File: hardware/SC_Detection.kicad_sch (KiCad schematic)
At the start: 86 parts, among them U15 LT1678CS8#PBF, U16 LT1678CS8#PBF, U17 LM211DRG4, U18 LM211DRG4, U19 LM211DRG4, U20 LM211DRG4

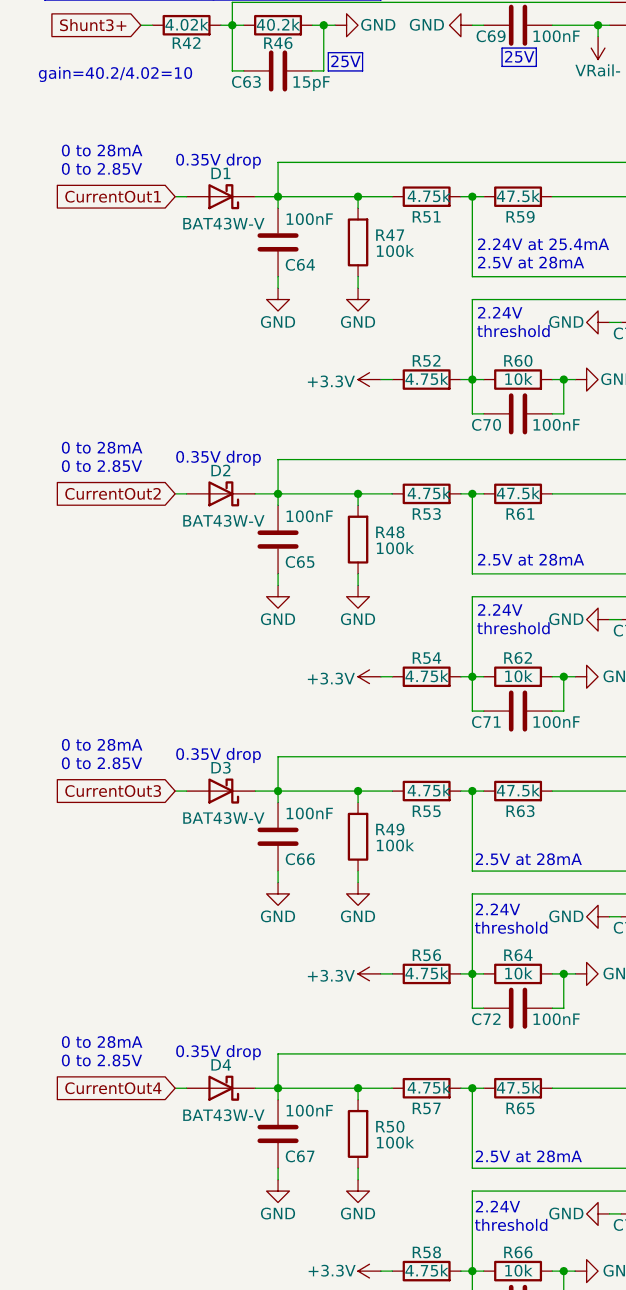
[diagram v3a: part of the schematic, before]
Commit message: Updating some footprints
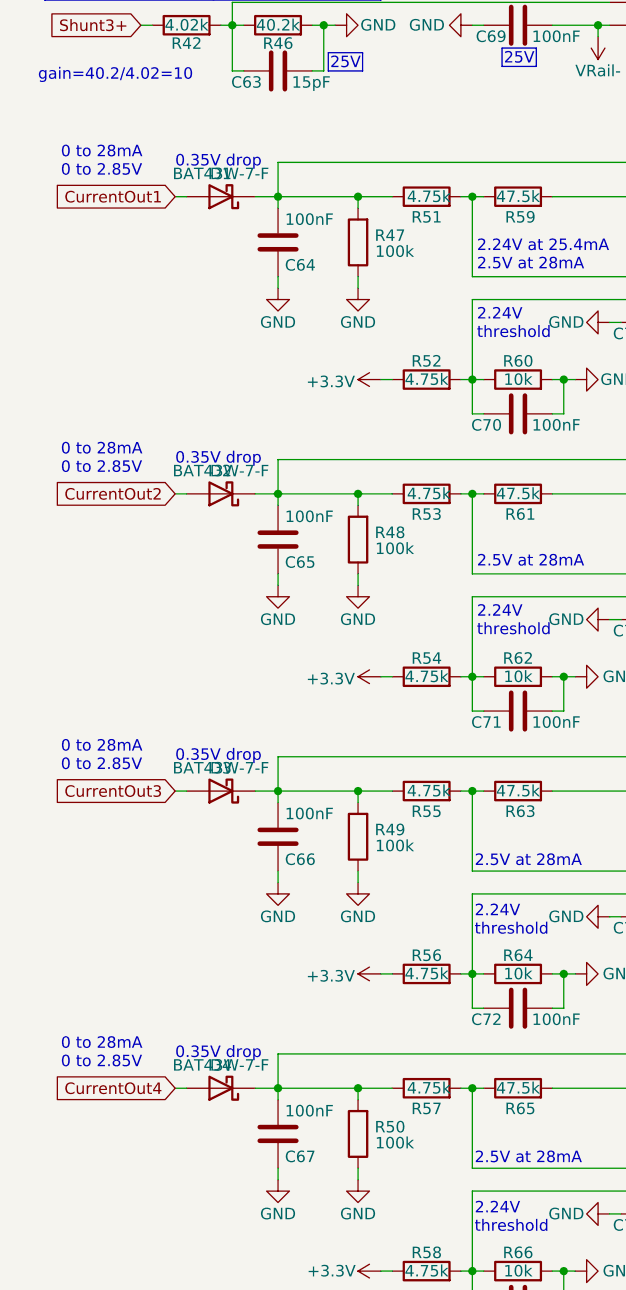
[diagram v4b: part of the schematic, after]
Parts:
- C60, C61, C62, C63, C64, C65, C66, C67, C68, C69, C70, C71, C72, C73, C74, C75, C76, C77, C78, C79, C80, C81, C82, C83, C84, C85, C86, C87, C88, C89, C90, C91: footprint Capacitor_SMD:C_0402_1005Metric -> Capacitor_SMD:C_0603_1608Metric; symbol harp.device.quad.dac:C -> harp.device.quad.dac:C_0603
- D1, D2, D3, D4: value BAT43W-V -> BAT43W-7-F
- R39, R40, R41, R42, R43, R44, R45, R46, R47, R48, R49, R50, R51, R52, R53, R54, R55, R56, R57, R58, R59, R60, R61, R62, R63, R64, R65, R66, R67, R68, R69, R70, R71, R72, R73, R74, R75, R76, R77, R78, R79, R80, R81, R82: footprint Resistor_SMD:R_0402_1005Metric -> Resistor_SMD:R_0603_1608Metric; symbol harp.device.quad.dac:R -> harp.device.quad.dac:R_0603
- U15, U16: footprint SOIC127P599X175-8N -> harp.device.quad.dac.kicad:SOIC127P599X175-8N
- U17, U18, U19, U20: footprint SOIC127P600X175-8N -> harp.device.quad.dac.kicad:SOIC127P600X175-8N

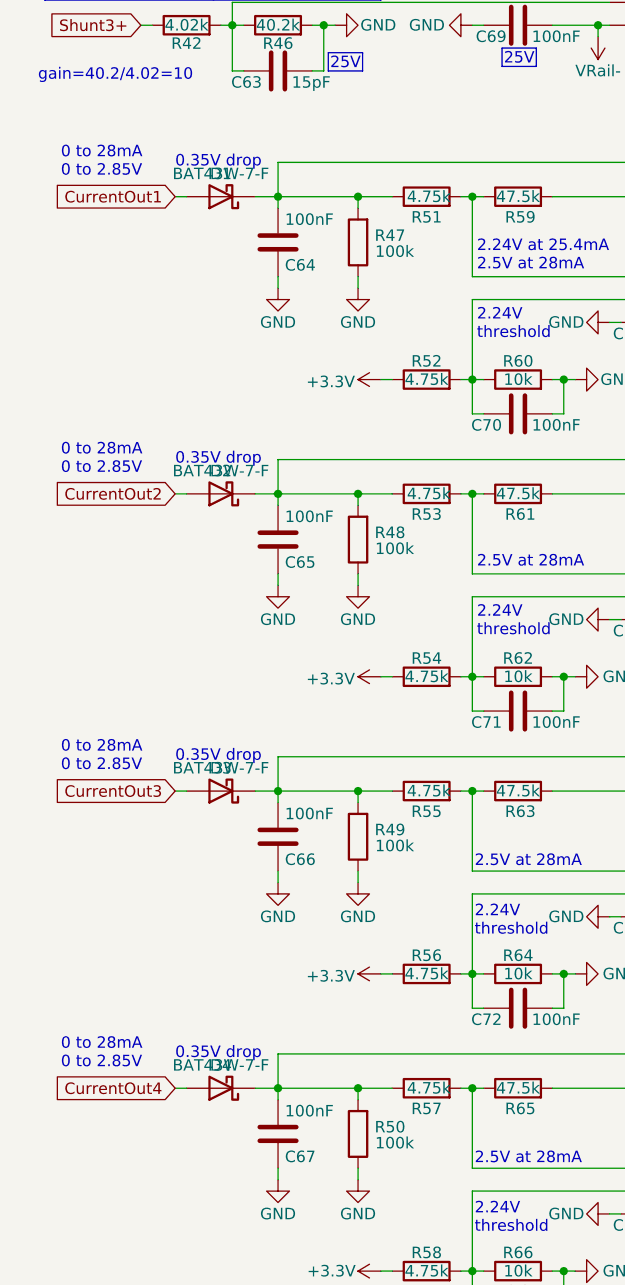
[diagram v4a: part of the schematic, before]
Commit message: Jumpers and interstages connections + added zeners to supply sections + justified text
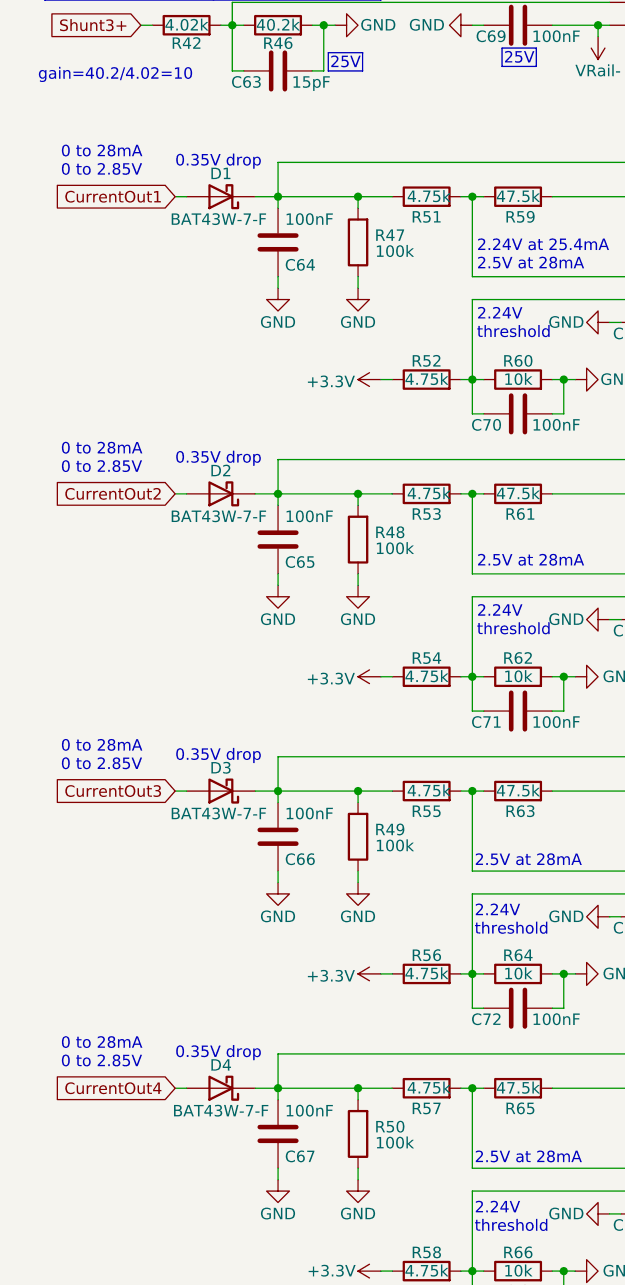
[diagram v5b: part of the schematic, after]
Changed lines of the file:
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@@
 		)
 		(property "Value" "BAT43W-7-F"
-			(at 33.02 168.91 0)
+			(at 33.02 173.99 0)
 			(effects
 				(font
@@
 		)
 		(property "Value" "BAT43W-7-F"
-			(at 33.02 135.89 0)
+			(at 32.766 140.97 0)
 			(effects
 				(font
@@
 		)
 		(property "Value" "BAT43W-7-F"
-			(at 33.02 69.85 0)
+			(at 32.766 74.93 0)
 			(effects
 				(font
@@
 		)
 		(property "Value" "BAT43W-7-F"
-			(at 33.02 102.87 0)
+			(at 32.766 107.95 0)
 			(effects
 				(font

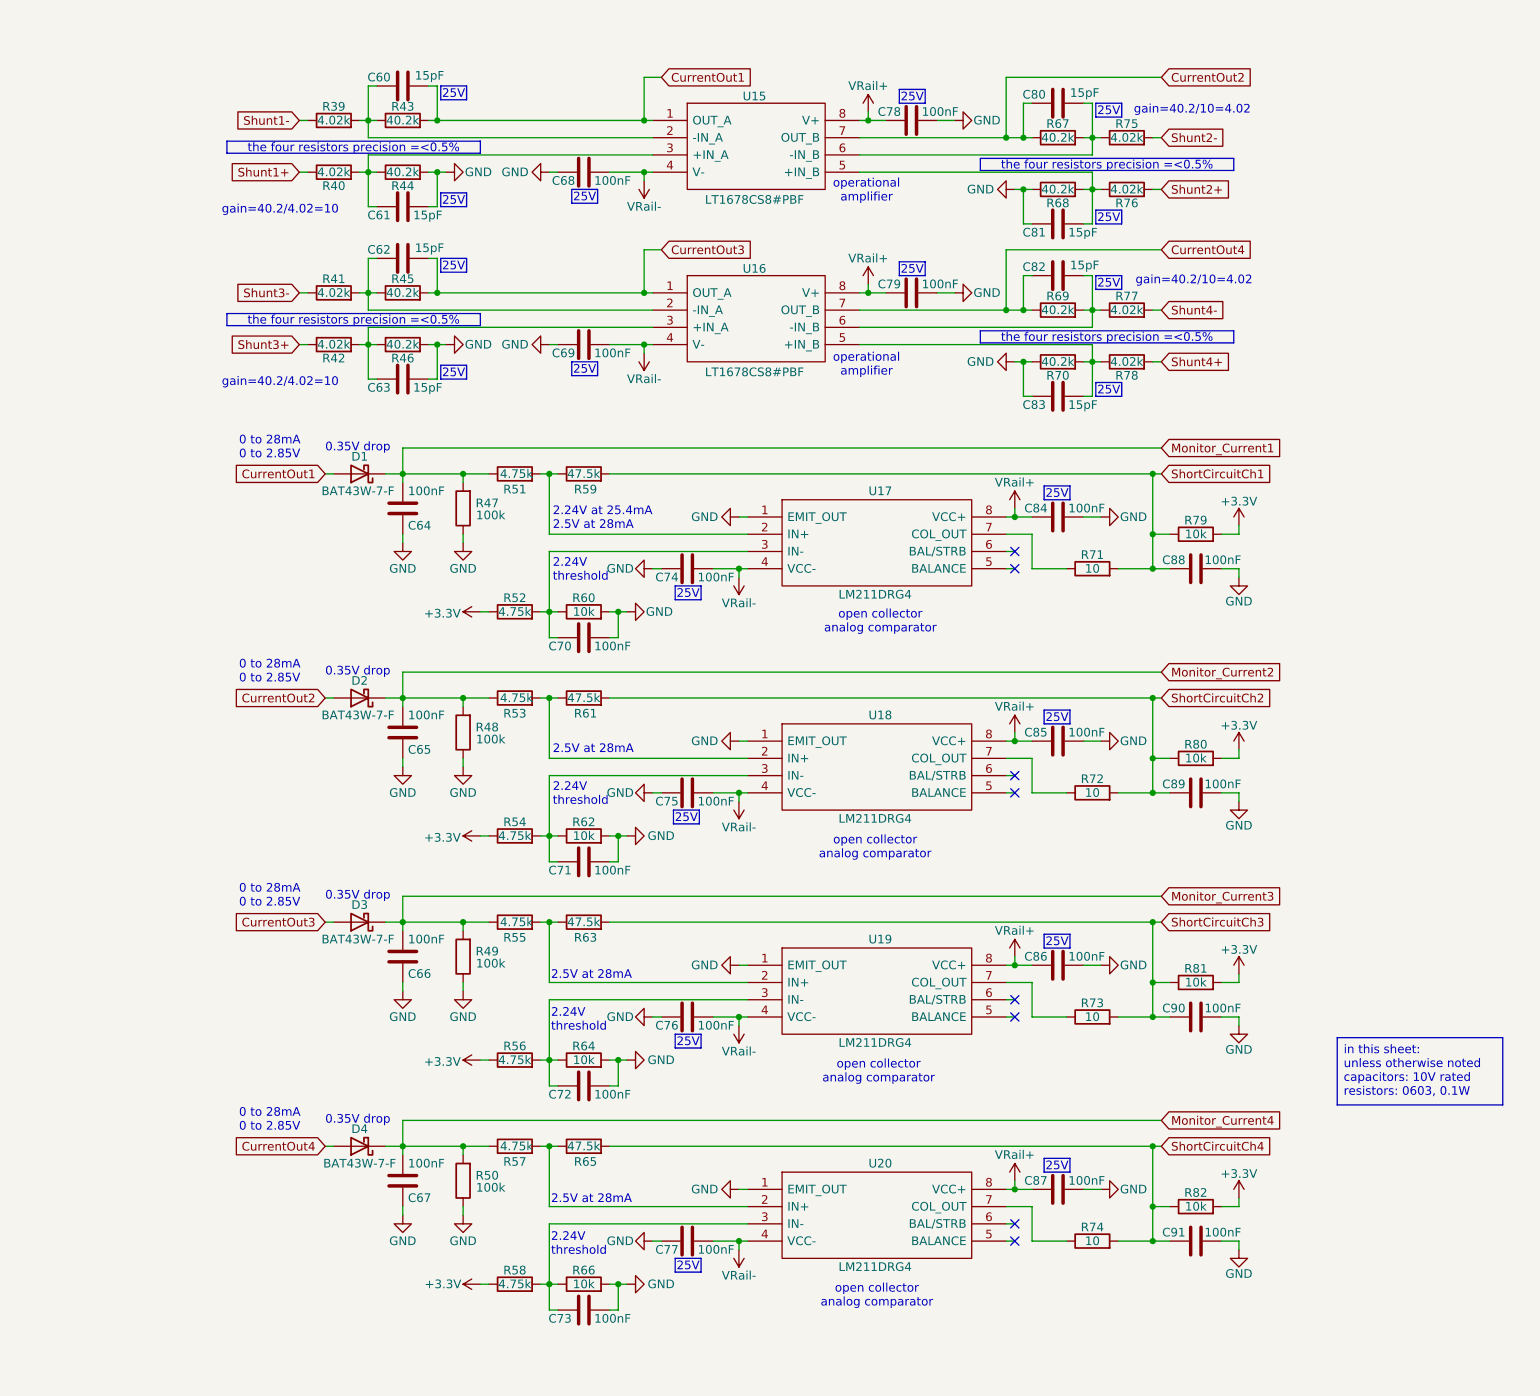
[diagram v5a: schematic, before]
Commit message: The part designators have been reannotated.
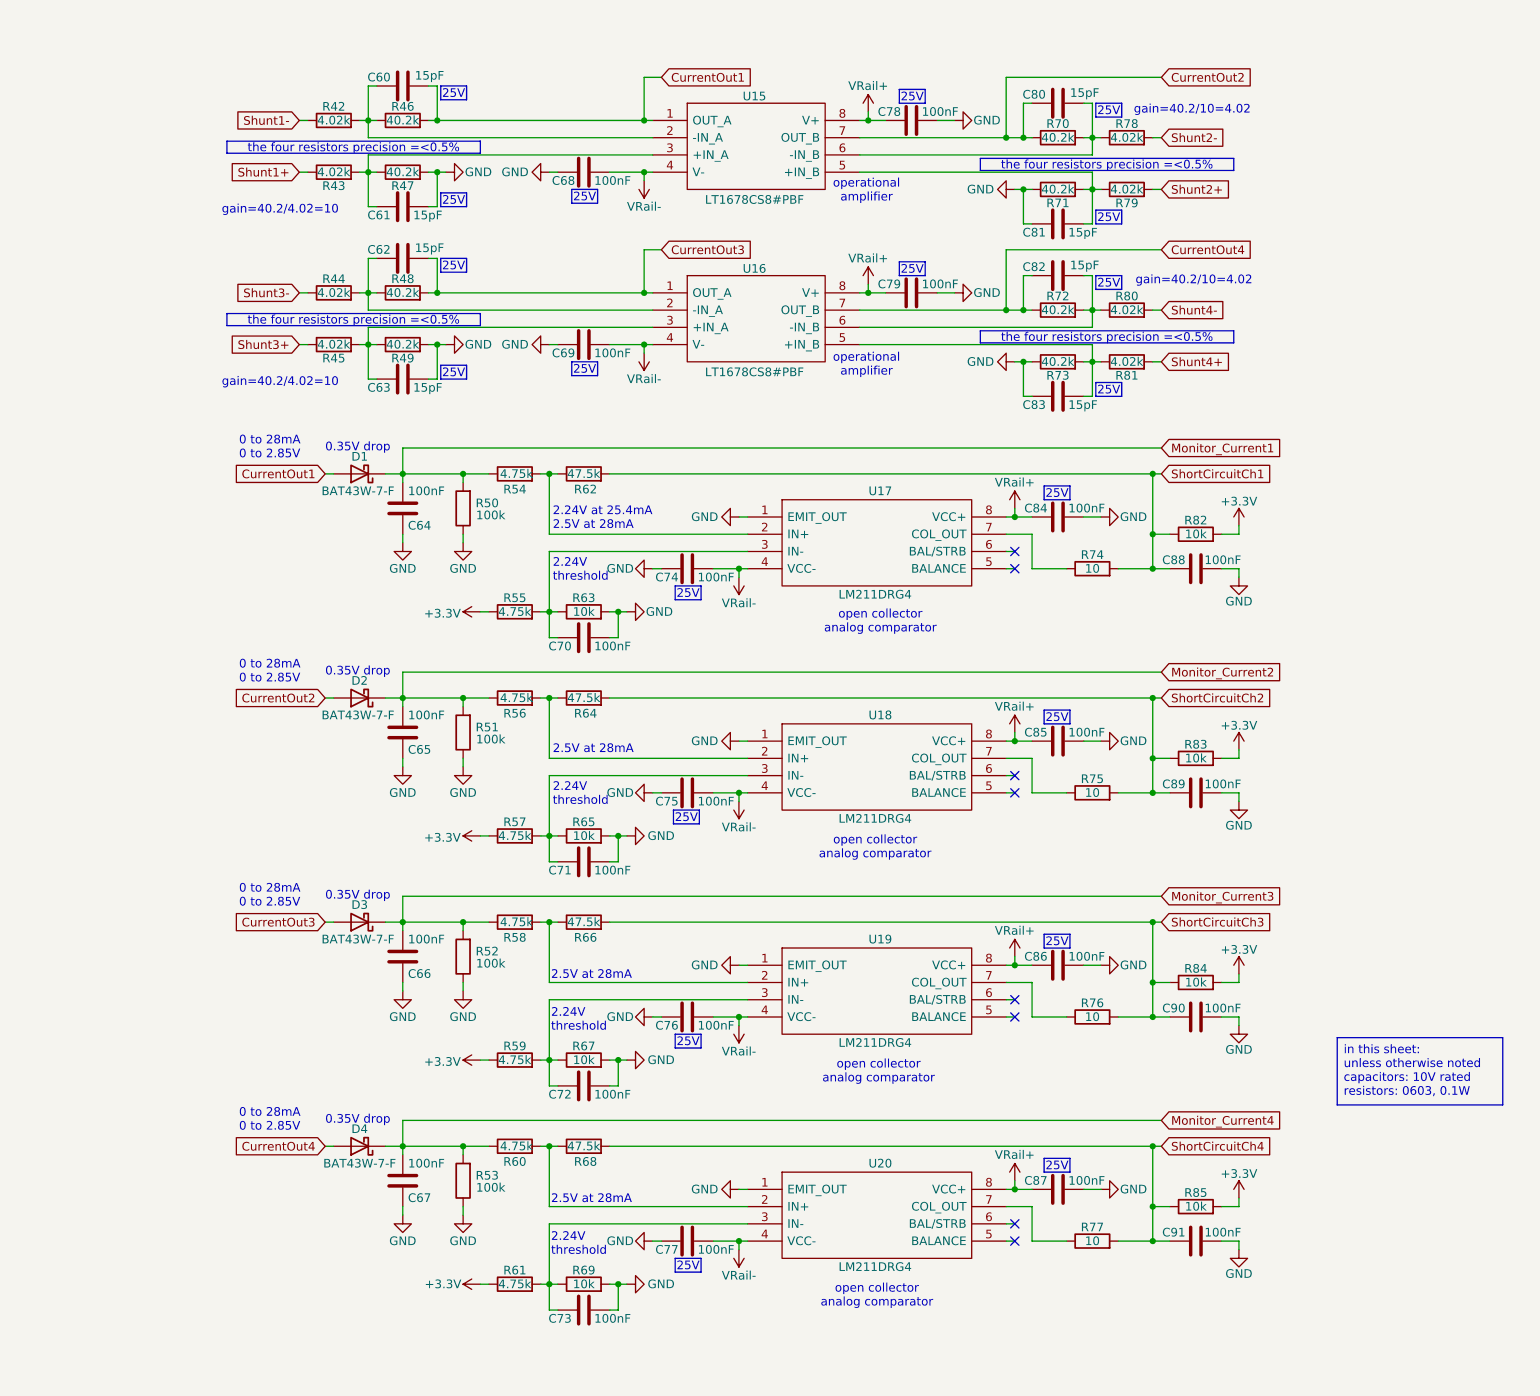
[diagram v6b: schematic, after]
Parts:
- renumbered R39 to R42, R40 to R43, R41 to R44, R42 to R45, R43 to R46, R44 to R47, R45 to R48, R46 to R49, R47 to R50, R48 to R51, R49 to R52, R50 to R53, R51 to R54, R52 to R55, R53 to R56, R54 to R57, R55 to R58, R56 to R59, R57 to R60, R58 to R61, R59 to R62, R60 to R63, R61 to R64, R62 to R65, R63 to R66, R64 to R67, R65 to R68, R66 to R69, R67 to R70, R68 to R71, R69 to R72, R70 to R73, R71 to R74, R72 to R75, R73 to R76, R74 to R77, R75 to R78, R76 to R79, R77 to R80, R78 to R81, R79 to R82, R80 to R83, R81 to R84, R82 to R85
